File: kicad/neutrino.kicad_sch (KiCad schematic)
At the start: 35 parts, among them K1 SW_Push, Q1 BTA16-800C, Q2 Q_NPN_BCE, Q3 Q_NPN_BCE, U1 TLP3023, U2 Rectifier, U3 ZT3L

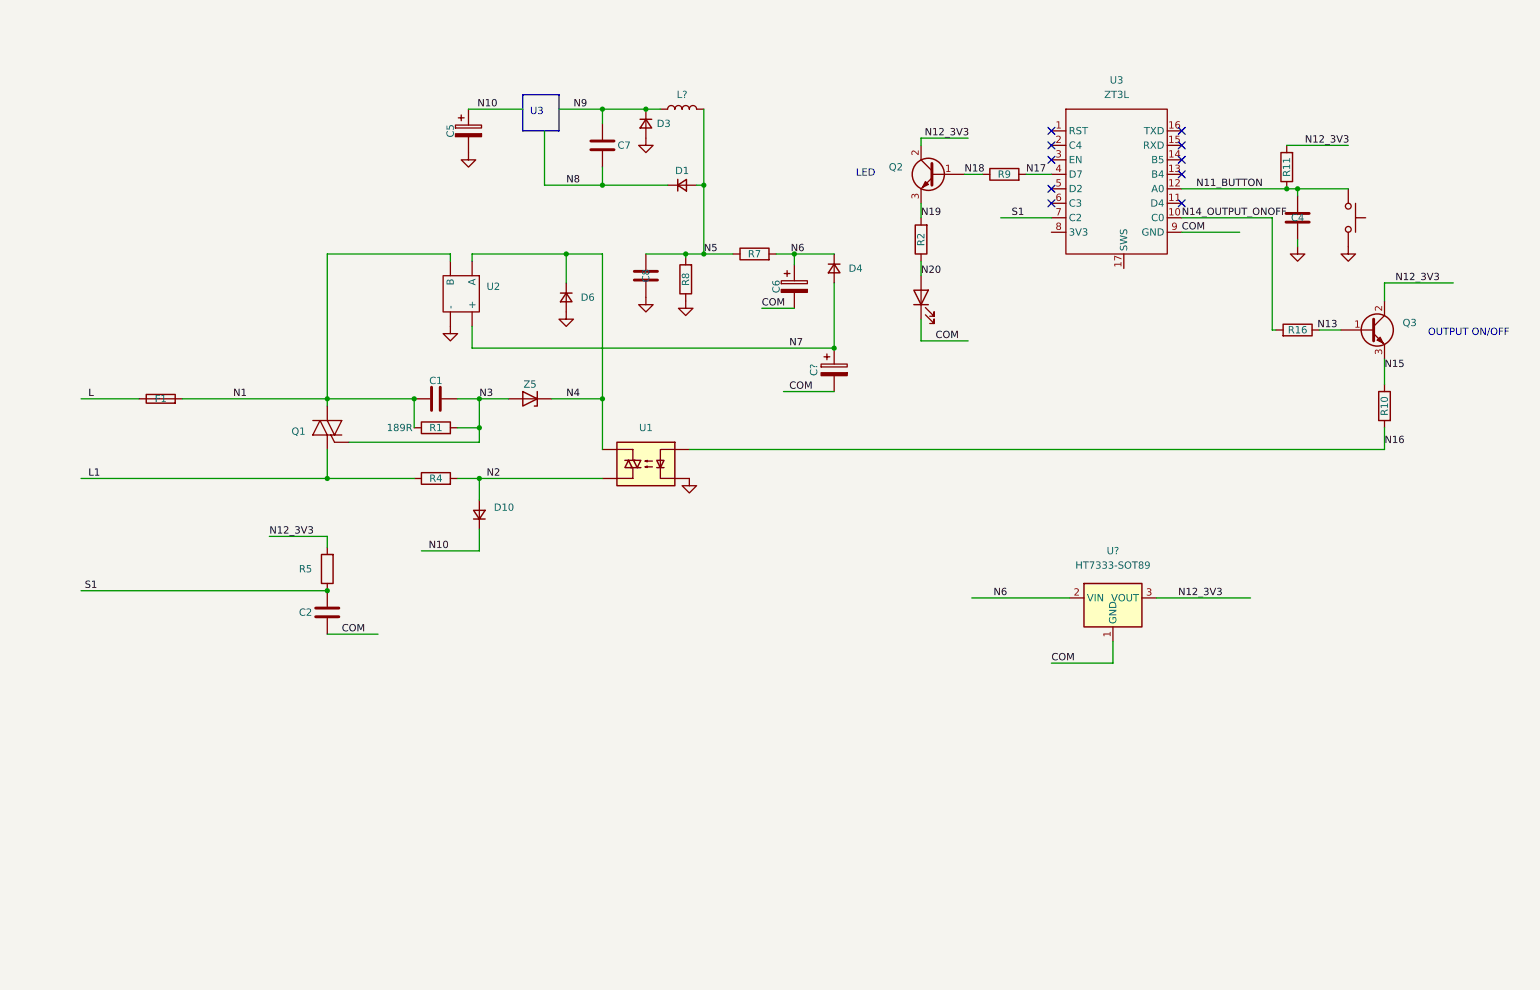
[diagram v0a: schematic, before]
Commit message: identified U3 as KP311A
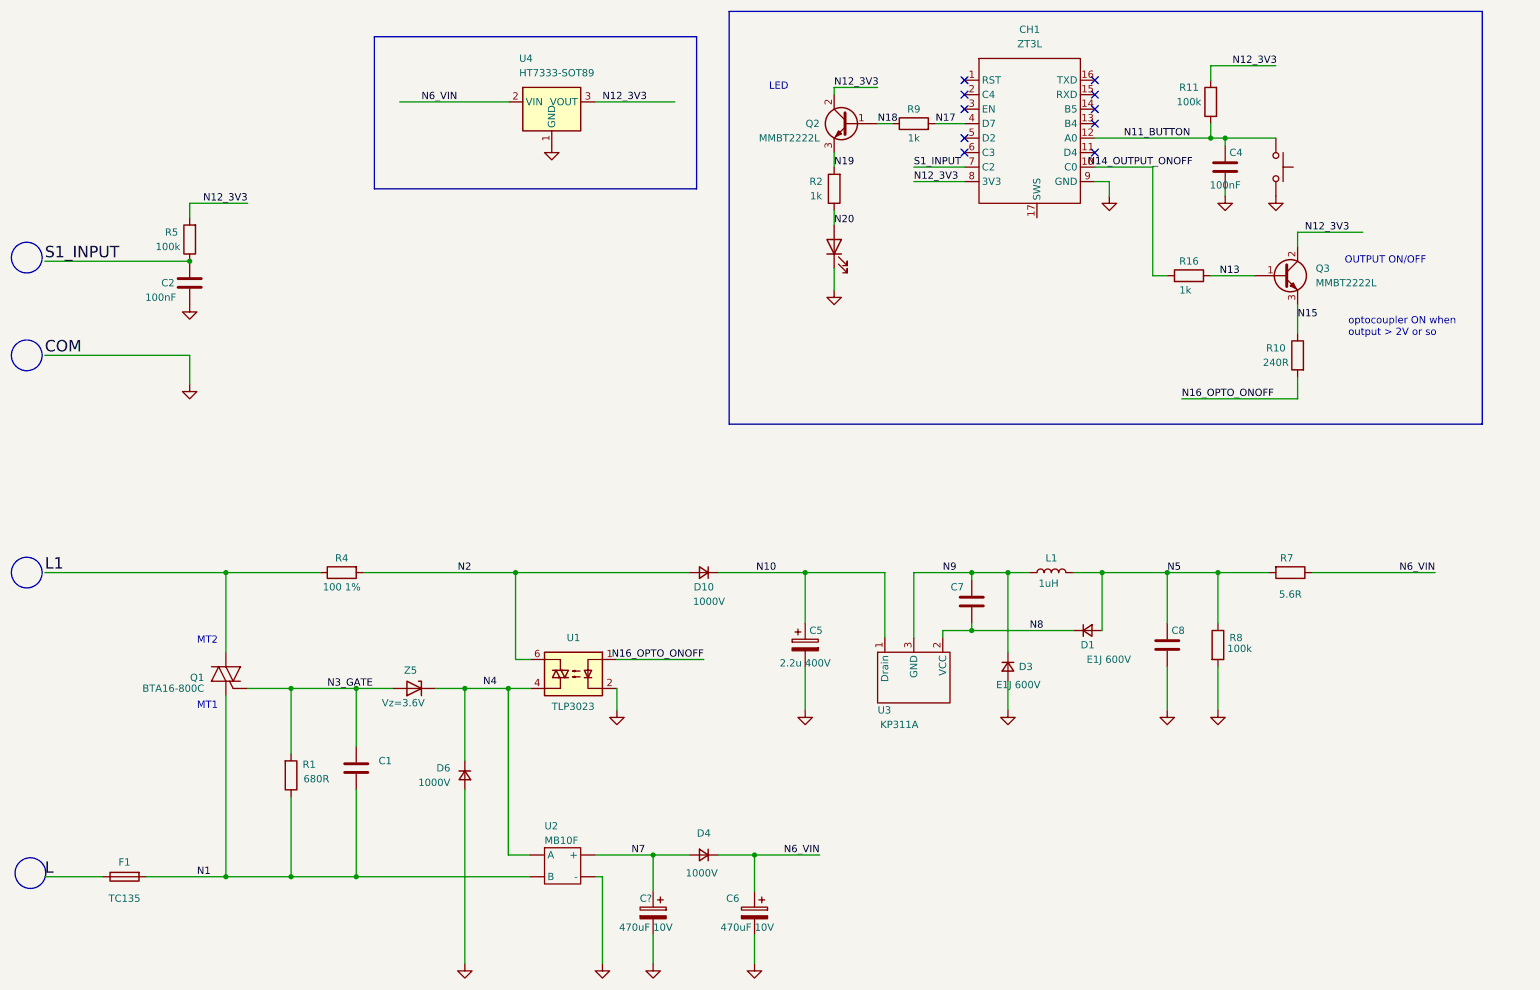
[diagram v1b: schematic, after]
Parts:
- added U3: KP311A, Package_TO_SOT_SMD:SOT-23, symbol neutrino:KP311A
- C2, C4: value C -> 100nF
- C5: value C_Polarized -> 2.2u 400V
- C6, C?: value C_Polarized -> 470uF 10V
- D1, D3: value D_Small -> E1J 600V
- D10, D6: value D_Small -> 1000V; Marking (none) -> A7
- D4: value D_Small -> 1000V; DC Blocking Voltage (none) -> 1000V; Marking (none) -> A7
- L1: renamed from L?; value L -> 1uH
- Q2, Q3: value Q_NPN_BCE -> MMBT2222L; Marking (none) -> 1P
- R1: value 189R -> 680R
- R10: value R -> 240R
- R11, R5, R8: value R -> 100k
- R16, R9: value R -> 1k
- R2: value R -> 1k; footprint (none) -> Resistor_SMD:R_0603_1608Metric
- R4: value R -> 100 1%; footprint Resistor_SMD:R_0402_1005Metric -> Resistor_SMD:R_MELF_MMB-0207; Type (none) -> MELF
- R7: value R -> 5.6R; Marking (none) -> 5R10
- U2: value Rectifier -> MB10F; Marking (none) -> MB10F
- Z5: value D_Zener -> Vz=3.6V; Marking (none) -> 4Z
- gave numbers to parts that had none: 1
- renumbered U3 to CH1
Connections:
- net COM is gone; now on net GND: C2.2, C6.2, C?.2, CH1.9 (GND), LED1.1 (K), U4.1 (GND)
- net GND: now also R8.2; no longer R8.1
- net L1: now also Q1.2 (A2); no longer Q1.1 (A1)
- net N1: now also Q1.1 (A1); no longer Q1.2 (A2)
- net N10: now also U3.1 (Drain)
- net N12_3V3: now also CH1.8 (3V3)
- net N14_OUTPUT_ONOFF: no longer CH1.10 (C0), R16.2
- net N2: now also U1.6; no longer U1.4
- net N4: no longer D6.1 (K), U1.6, U2. (B), Z5.1 (K)
- net N5: now also R7.2, R8.1; no longer R7.1, R8.2
- net N8: now also U3.2 (VCC)
- net N9: now also U3.3 (GND)
- net N16 renamed N16_OPTO_ONOFF
- net N3 renamed N3_GATE
- net N6 renamed N6_VIN
- net N6_VIN: now also R7.1; no longer R7.2
- net S1 renamed S1_INPUT
- new net: CH1.10 (C0), R16.2
- new net: D6.1 (K), U1.4, U2. (B), Z5.1 (K)
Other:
- note added: "MT1"
- note added: "MT2"
- note added: "optocoupler ON when output > 2V or so"
- note removed: "U3"
- moved on the sheet: C1, C2, C4, C5, C6, C7, C8, C?, CH1, D1, D10, D3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
